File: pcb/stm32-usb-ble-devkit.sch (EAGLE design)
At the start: 91 parts, among them CN1 USB-MICROB-2TABS, CN2 USB-C-2.0-FEMALE, CN3 USB-C-2.0-FEMALE, Q2 AO3402, Q4 AO3401, Q6 AO3401, Q8 AO3401, U1 STM32F103-48LQFP, U2 STM32F205-64, U3 TUSB320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

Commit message: pcb: Fix symbol orientation and add PSU caps
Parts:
- added C20, C21: 100n, tuetuopay:C0805
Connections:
- net +3V3: now also C21.1
- net +5V: now also C20.1
- net GND: now also C20.2, C21.2
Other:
- moved on the sheet: C17

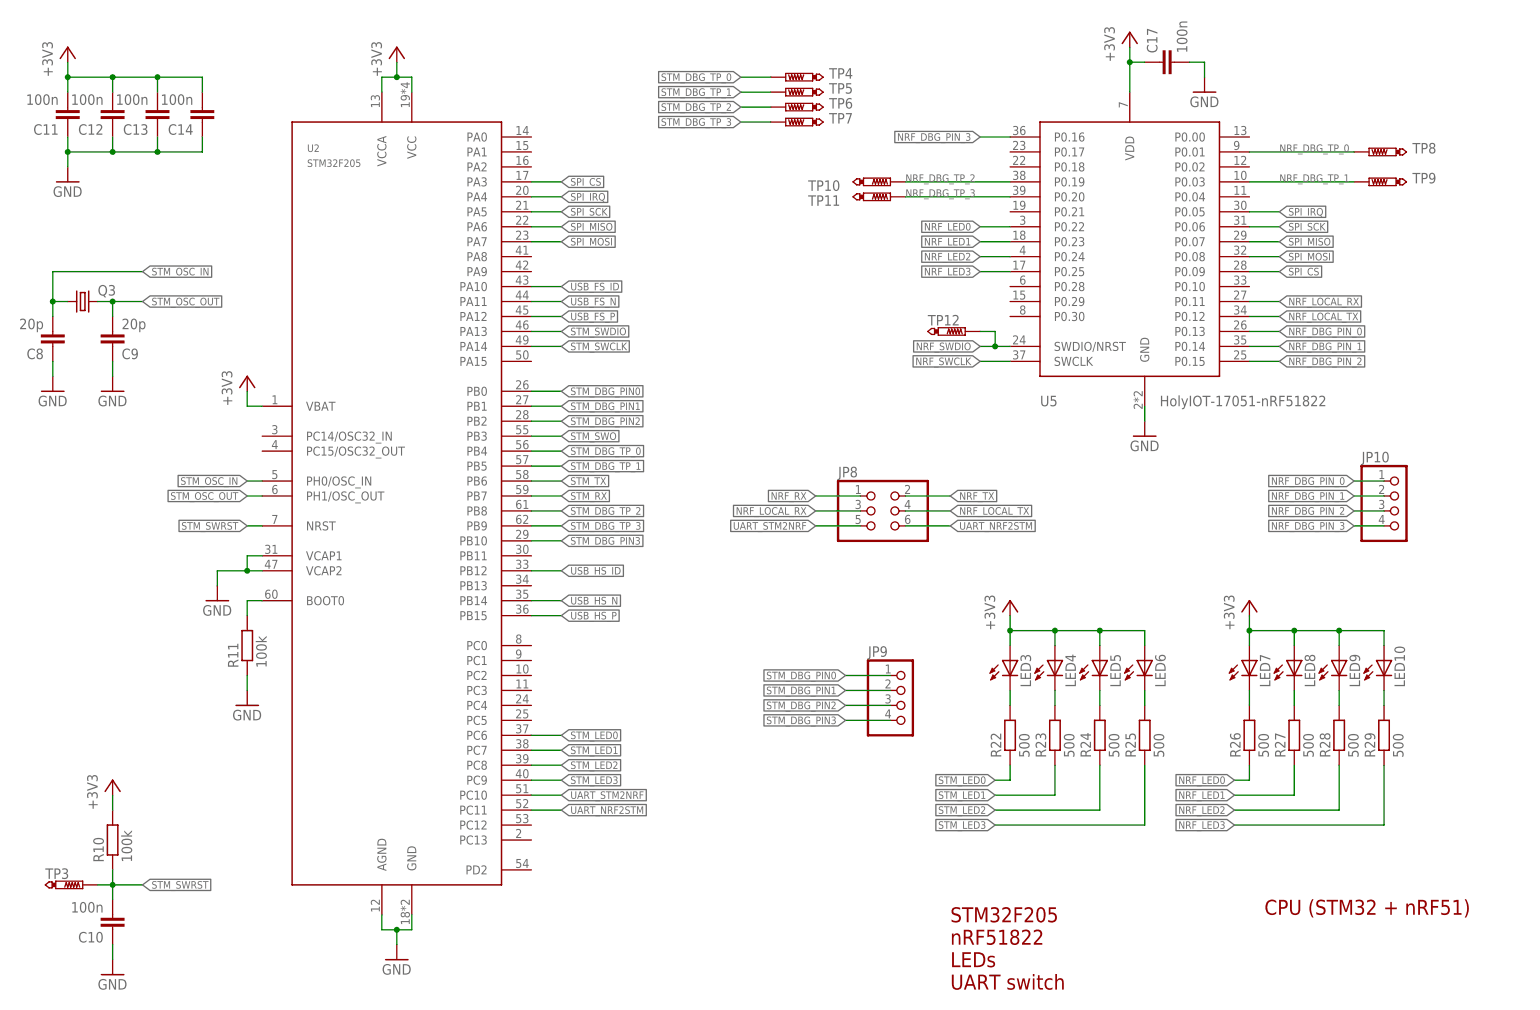
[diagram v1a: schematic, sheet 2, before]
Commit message: pcb: Add SPI PU/PD resistors
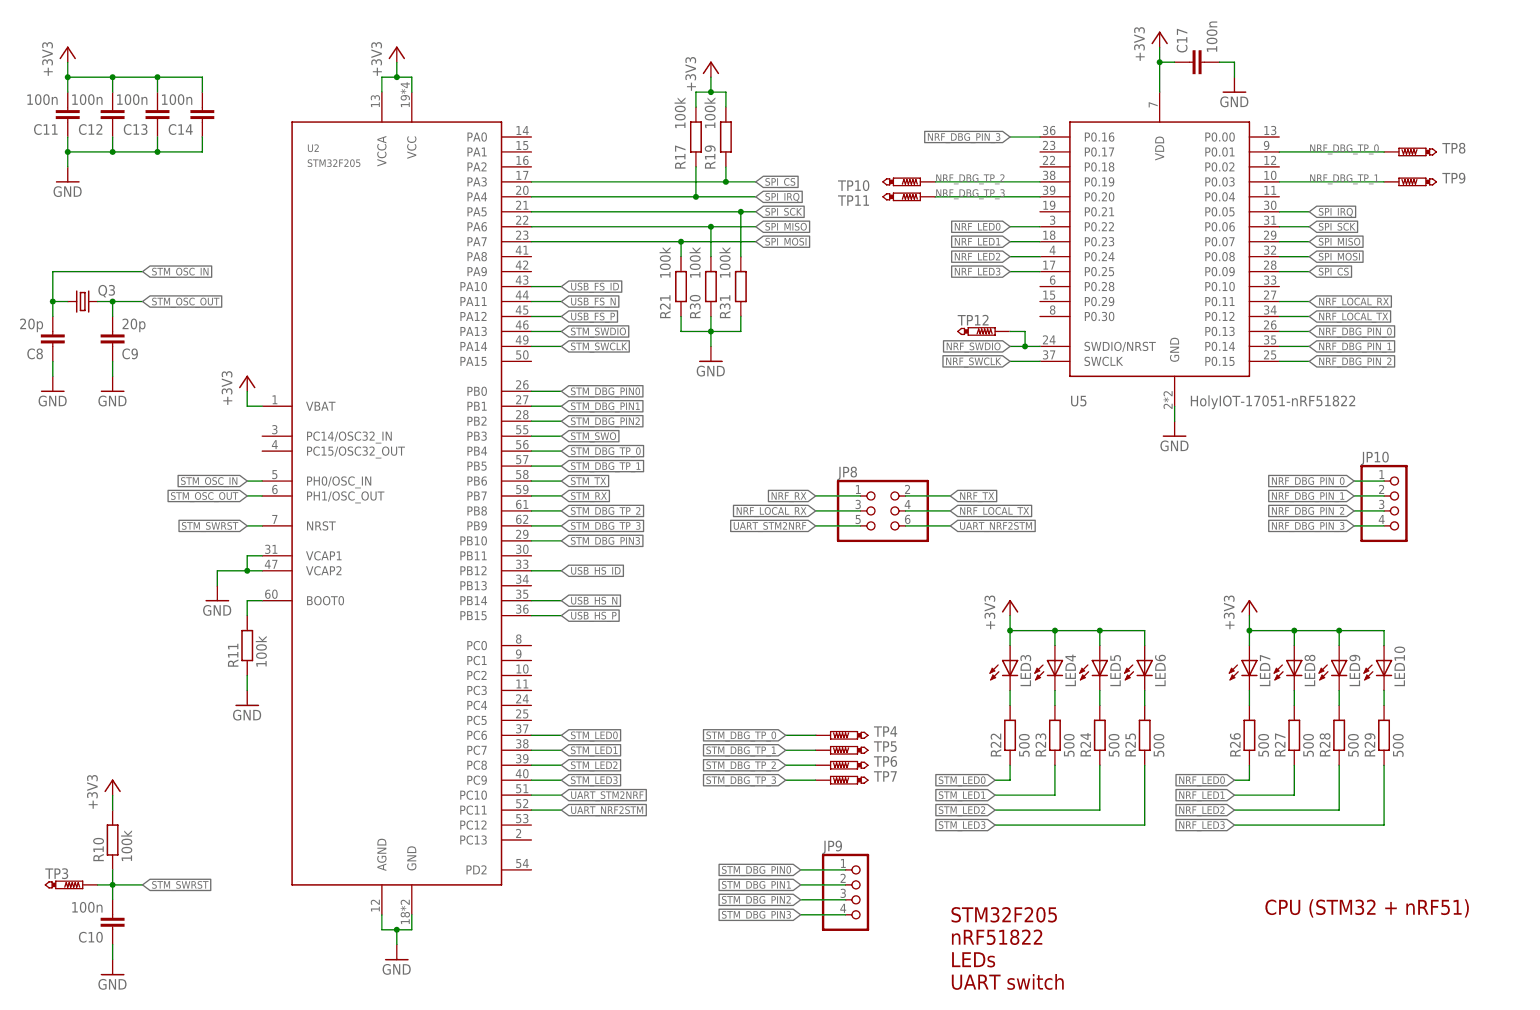
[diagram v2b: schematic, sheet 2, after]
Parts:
- added R17, R19, R21, R30, R31: 100k, tuetuopay:RR0603
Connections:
- net +3V3: now also R17.2, R19.2
- net GND: now also R21.1, R30.1, R31.1
- net SPI_CS: now also R19.1
- net SPI_IRQ: now also R17.1
- net SPI_MISO: now also R30.2
- net SPI_MOSI: now also R21.2
- net SPI_SCK: now also R31.2
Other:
- moved on the sheet: C17, JP9, TP10, TP11, TP12, TP4, TP5, TP6, TP7, TP8, TP9, U5

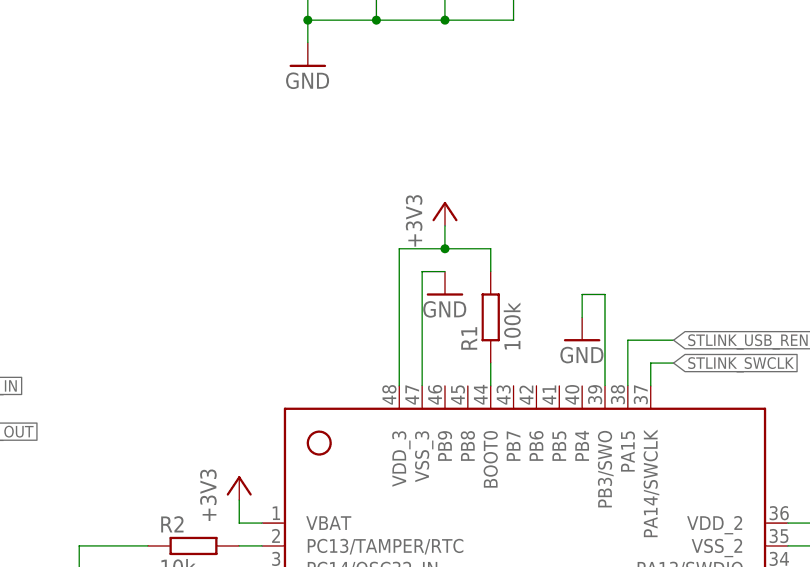
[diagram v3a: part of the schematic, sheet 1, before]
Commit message: pcb: Fix ST-LINK BOOT0 resistor
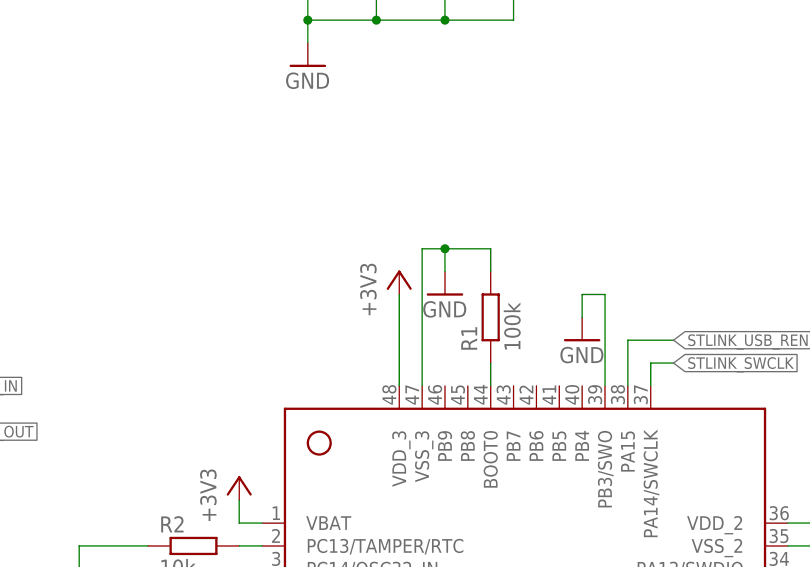
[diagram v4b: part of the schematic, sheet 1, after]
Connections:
- net +3V3: no longer R1.2
- net GND: now also R1.2
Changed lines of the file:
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@@
 <part name="GND17" library="supply1" library_urn="urn:adsk.eagle:library:371" deviceset="GND" device=""/>
 <part name="R11" library="tuetuopay" deviceset="R" device="R0603" value="100k"/>
-<part name="GND18" library="supply1" library_urn="urn:adsk.eagle:library:371" deviceset="GND" device=""/>
 <part name="TP4" library="testpad" library_urn="urn:adsk.eagle:library:385" deviceset="PTR1" device="B1,27" package3d_urn="urn:adsk.eagle:package:27944/1"/>
 <part name="TP5" library="testpad" library_urn="urn:adsk.eagle:library:385" deviceset="PTR1" device="B1,27" package3d_urn="urn:adsk.eagle:package:27944/1"/>
@@
 <instance part="U1" gate="G$1" x="111.76" y="76.2"/>
 <instance part="R1" gate="G$1" x="106.68" y="111.76" rot="R90"/>
-<instance part="+3V1" gate="G$1" x="101.6" y="124.46"/>
+<instance part="+3V1" gate="G$1" x="96.52" y="116.84"/>
 <instance part="+3V2" gate="G$1" x="55.88" y="71.12"/>
 <instance part="+3V3" gate="G$1" x="132.08" y="45.72"/>
@@
 <net name="+3V3" class="0">
 <segment>
-<pinref part="U1" gate="G$1" pin="VDD_3"/>
-<wire x1="96.52" y1="104.14" x2="96.52" y2="119.38" width="0.1524" layer="91"/>
-<wire x1="96.52" y1="119.38" x2="101.6" y2="119.38" width="0.1524" layer="91"/>
-<pinref part="R1" gate="G$1" pin="2"/>
-<wire x1="101.6" y1="119.38" x2="106.68" y2="119.38" width="0.1524" layer="91"/>
-<wire x1="106.68" y1="119.38" x2="106.68" y2="116.84" width="0.1524" layer="91"/>
-<pinref part="+3V1" gate="G$1" pin="+3V3"/>
-<wire x1="101.6" y1="121.92" x2="101.6" y2="119.38" width="0.1524" layer="91"/>
-<junction x="101.6" y="119.38"/>
-</segment>
-<segment>
 <pinref part="+3V2" gate="G$1" pin="+3V3"/>
 <pinref part="U1" gate="G$1" pin="VDDA"/>
@@
 <wire x1="25.4" y1="167.64" x2="25.4" y2="165.1" width="0.1524" layer="91"/>
 </segment>
+<segment>
+<pinref part="U1" gate="G$1" pin="VDD_3"/>
+<wire x1="96.52" y1="104.14" x2="96.52" y2="114.3" width="0.1524" layer="91"/>
+<pinref part="+3V1" gate="G$1" pin="+3V3"/>
+</segment>
 </net>
 <net name="GND" class="0">
-<segment>
-<pinref part="GND4" gate="1" pin="GND"/>
-<pinref part="U1" gate="G$1" pin="VSS_3"/>
-<wire x1="101.6" y1="116.84" x2="99.06" y2="116.84" width="0.1524" layer="91"/>
-<wire x1="99.06" y1="116.84" x2="99.06" y2="104.14" width="0.1524" layer="91"/>
-</segment>
 <segment>
 <pinref part="GND3" gate="1" pin="GND"/>
@@
 <wire x1="119.38" y1="114.3" x2="119.38" y2="104.14" width="0.1524" layer="91"/>
 </segment>
-</net>
+<segment>
+<pinref part="U1" gate="G$1" pin="VSS_3"/>
+<wire x1="99.06" y1="119.38" x2="99.06" y2="104.14" width="0.1524" layer="91"/>
+<wire x1="99.06" y1="119.38" x2="101.6" y2="119.38" width="0.1524" layer="91"/>
+<pinref part="R1" gate="G$1" pin="2"/>
+<wire x1="101.6" y1="119.38" x2="106.68" y2="119.38" width="0.1524" layer="91"/>
+<wire x1="106.68" y1="119.38" x2="106.68" y2="116.84" width="0.1524" layer="91"/>
+<pinref part="GND4" gate="1" pin="GND"/>
+<wire x1="101.6" y1="116.84" x2="101.6" y2="119.38" width="0.1524" layer="91"/>
+<junction x="101.6" y="119.38"/>
+</segment>
+</net>

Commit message: pcb: Fix STM32 VCAP pins
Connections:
- net GND: no longer U2.VCAP1, U2.VCAP2
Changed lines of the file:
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@@
 <instance part="GND17" gate="1" x="45.72" y="55.88"/>
 <instance part="R11" gate="G$1" x="45.72" y="66.04" rot="R90"/>
-<instance part="GND18" gate="1" x="40.64" y="73.66"/>
 <instance part="TP4" gate="G$1" x="144.78" y="50.8" smashed="yes" rot="R90">
 <attribute name="NAME" x="156.21" y="52.324" size="1.778" layer="95" rot="R180"/>
@@
 </segment>
 <segment>
-<pinref part="GND18" gate="1" pin="GND"/>
-<pinref part="U2" gate="G$1" pin="VCAP2"/>
-<wire x1="40.64" y1="76.2" x2="40.64" y2="78.74" width="0.1524" layer="91"/>
-<wire x1="40.64" y1="78.74" x2="45.72" y2="78.74" width="0.1524" layer="91"/>
-<pinref part="U2" gate="G$1" pin="VCAP1"/>
-<wire x1="45.72" y1="78.74" x2="48.26" y2="78.74" width="0.1524" layer="91"/>
-<wire x1="45.72" y1="78.74" x2="45.72" y2="81.28" width="0.1524" layer="91"/>
-<wire x1="45.72" y1="81.28" x2="48.26" y2="81.28" width="0.1524" layer="91"/>
-<junction x="45.72" y="78.74"/>
-</segment>
-<segment>

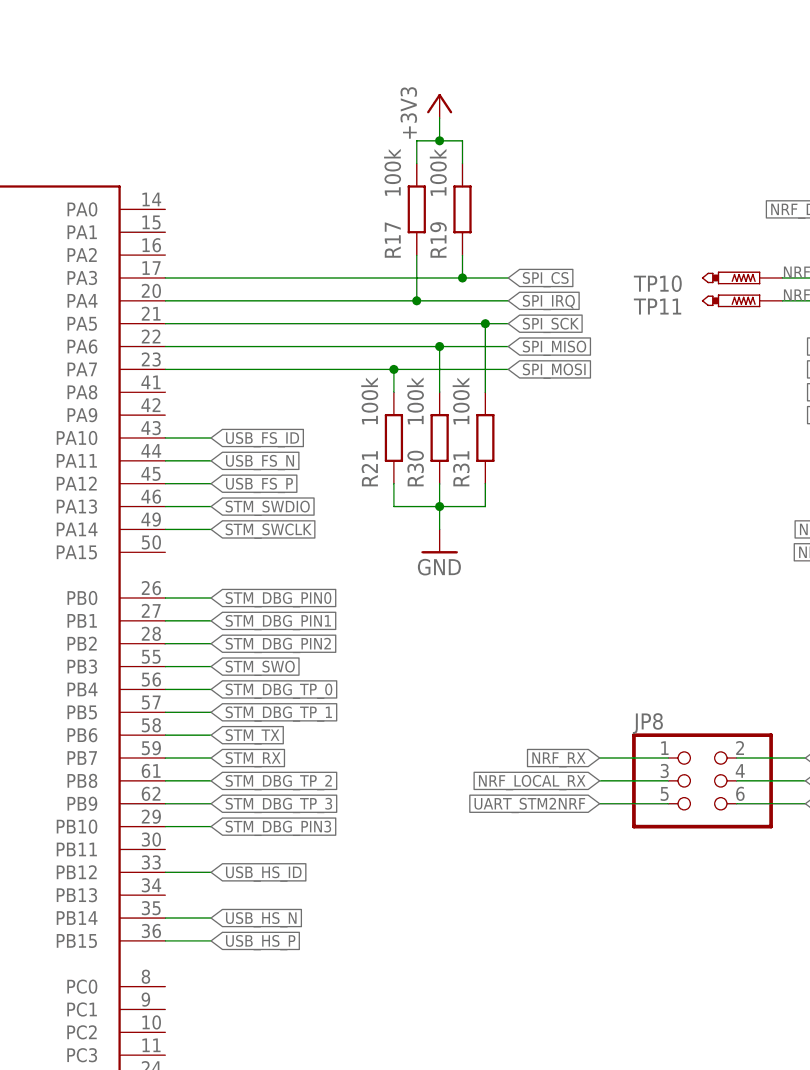
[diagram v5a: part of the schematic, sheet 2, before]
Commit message: pcb: Add USB VBUS detection and USB BUS ON
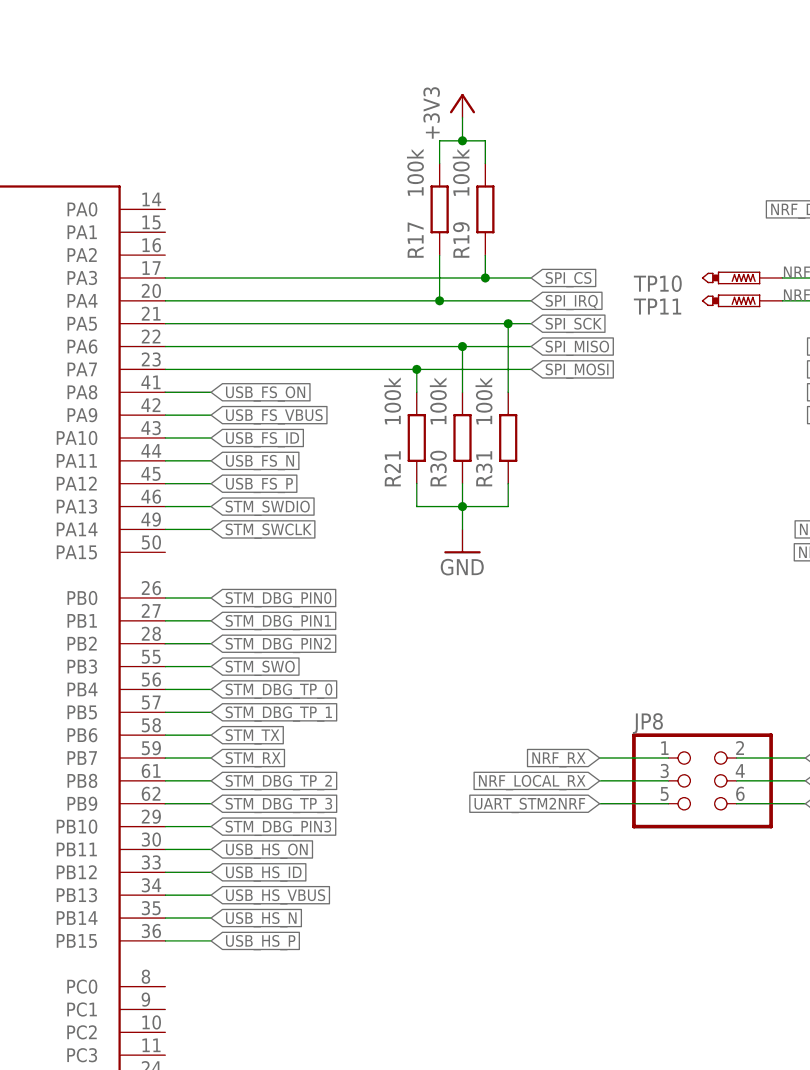
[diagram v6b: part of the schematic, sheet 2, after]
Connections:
- new net USB_FS_ON: Q6.G, U2.PA8
- new net USB_HS_ON: Q8.G, U2.PB11
- net USB_FS_ID: no longer Q6.G
- net USB_FS_VBUS: now also U2.PA9
- net USB_HS_ID: no longer Q8.G
- net USB_HS_VBUS: now also U2.PB13
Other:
- moved on the sheet: R17, R19, R21, R30, R31

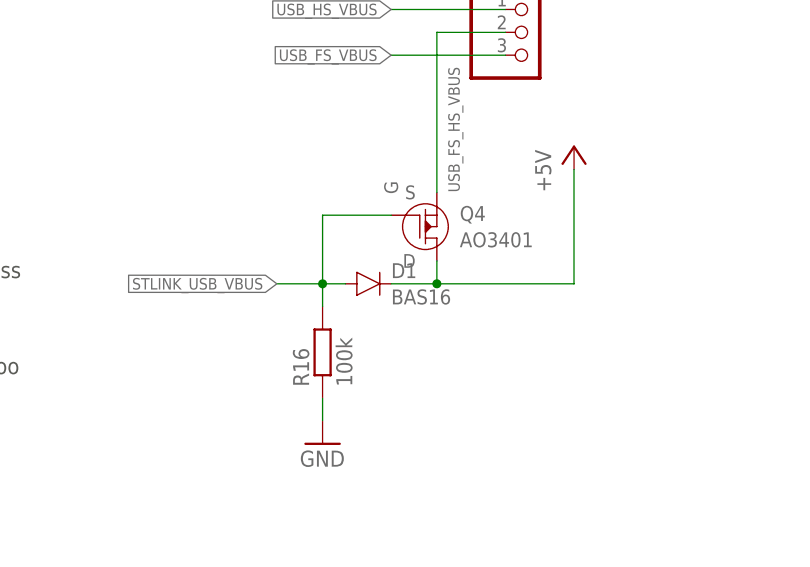
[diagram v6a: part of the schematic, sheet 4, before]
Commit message: pcb: Replaced PSU BAS16 with better diode
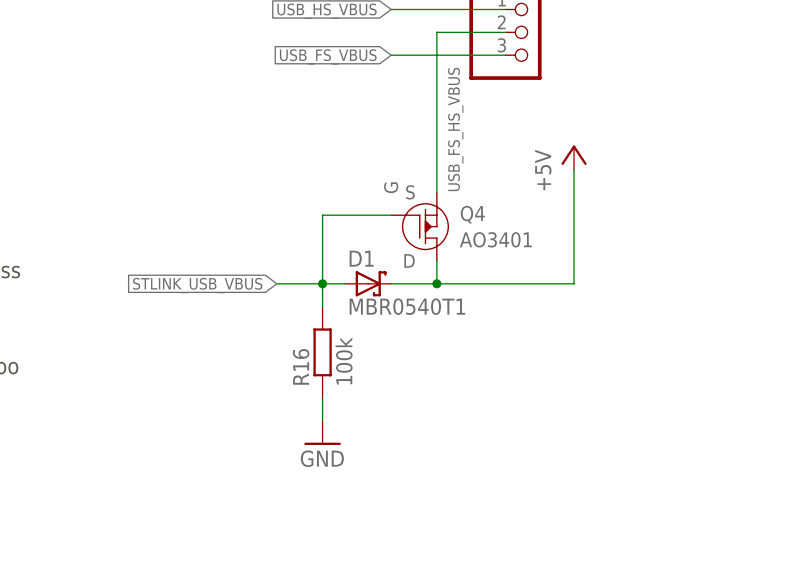
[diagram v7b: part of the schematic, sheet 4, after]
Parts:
- D1: value BAS16 -> MBR0540T1; device tuetuopay:BAS16 -> tuetuopay:MBR0540T1
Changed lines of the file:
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@@
 <part name="FRAME4" library="frames" library_urn="urn:adsk.eagle:library:229" deviceset="A4L-LOC" device=""/>
 <part name="Q4" library="tuetuopay" deviceset="AO3401" device=""/>
-<part name="D1" library="tuetuopay" deviceset="BAS16" device=""/>
 <part name="R16" library="tuetuopay" deviceset="R" device="R0603" value="100k"/>
 <part name="GND27" library="supply1" library_urn="urn:adsk.eagle:library:371" deviceset="GND" device=""/>
@@
 <part name="+3V19" library="supply1" library_urn="urn:adsk.eagle:library:371" deviceset="+3V3" device=""/>
 <part name="GND28" library="supply1" library_urn="urn:adsk.eagle:library:371" deviceset="GND" device=""/>
+<part name="D1" library="tuetuopay" deviceset="MBR0540T1" device=""/>
 </parts>
 <sheets>
@@
 <instance part="FRAME4" gate="G$1" x="0" y="0"/>
 <instance part="Q4" gate="G$1" x="83.82" y="106.68"/>
-<instance part="D1" gate="G$1" x="76.2" y="101.6"/>
 <instance part="R16" gate="G$1" x="71.12" y="93.98" rot="R90"/>
 <instance part="GND27" gate="1" x="71.12" y="83.82"/>
@@
 <instance part="C20" gate="&gt;NAME" x="38.1" y="30.48" rot="MR0"/>
 <instance part="C21" gate="&gt;NAME" x="83.82" y="30.48"/>
+<instance part="D1" gate="G$1" x="76.2" y="101.6"/>
 </instances>
 <busses>
@@
 <wire x1="71.12" y1="101.6" x2="71.12" y2="109.22" width="0.1524" layer="91"/>
 <wire x1="71.12" y1="109.22" x2="78.74" y2="109.22" width="0.1524" layer="91"/>
-<pinref part="D1" gate="G$1" pin="A"/>
-<wire x1="71.12" y1="101.6" x2="73.66" y2="101.6" width="0.1524" layer="91"/>
 <junction x="71.12" y="101.6"/>
 <wire x1="71.12" y1="101.6" x2="66.04" y2="101.6" width="0.1524" layer="91"/>
 <label x="66.04" y="101.6" size="1.27" layer="95" rot="R180" xref="yes"/>
+<pinref part="D1" gate="G$1" pin="A"/>
+<wire x1="73.66" y1="101.6" x2="71.12" y2="101.6" width="0.1524" layer="91"/>
 </segment>
 </net>
@@
 </segment>
 <segment>
-<pinref part="D1" gate="G$1" pin="C"/>
-<wire x1="78.74" y1="101.6" x2="83.82" y2="101.6" width="0.1524" layer="91"/>
 <pinref part="Q4" gate="G$1" pin="D"/>
 <wire x1="83.82" y1="101.6" x2="83.82" y2="104.14" width="0.1524" layer="91"/>
 <wire x1="83.82" y1="101.6" x2="99.06" y2="101.6" width="0.1524" layer="91"/>
-<junction x="83.82" y="101.6"/>
 <pinref part="P+1" gate="1" pin="+5V"/>
 <wire x1="99.06" y1="101.6" x2="99.06" y2="114.3" width="0.1524" layer="91"/>
-</segment>
-<segment>
+<pinref part="D1" gate="G$1" pin="C"/>
+<wire x1="78.74" y1="101.6" x2="83.82" y2="101.6" width="0.1524" layer="91"/>
+<junction x="83.82" y="101.6"/>
+</segment>
+<segment>
